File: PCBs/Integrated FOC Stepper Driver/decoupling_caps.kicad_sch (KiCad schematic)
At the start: 12 parts

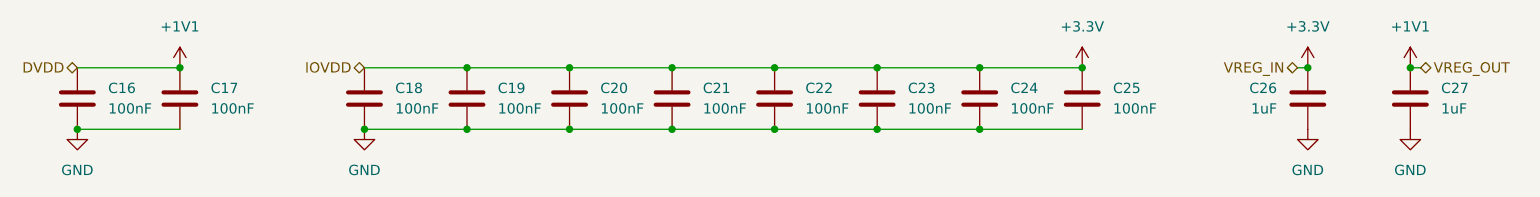
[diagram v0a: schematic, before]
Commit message: Switch to 0805 capacitors instead of stacked 2220 capacitors
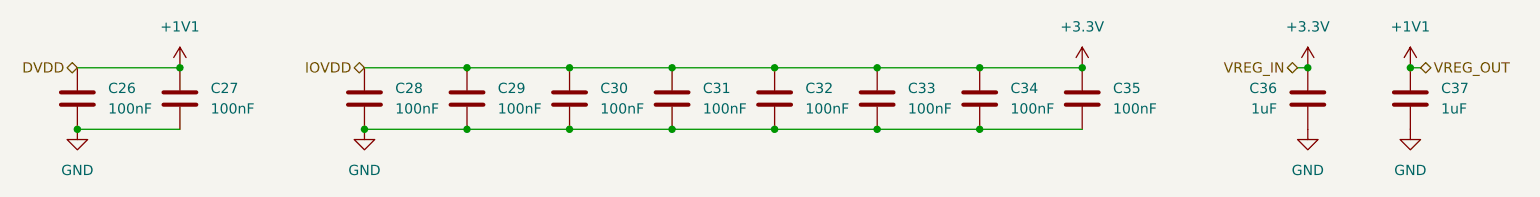
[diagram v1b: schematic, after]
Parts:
- renumbered C16 to C26, C17 to C27, C18 to C28, C19 to C29, C20 to C30, C21 to C31, C22 to C32, C23 to C33, C24 to C34, C25 to C35, C26 to C36, C27 to C37
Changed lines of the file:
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@@
 (kicad_sch
-	(version 20231120)
+	(version 20250114)
 	(generator "eeschema")
-	(generator_version "8.0")
+	(generator_version "9.0")
 	(paper "A4")
 	(junction
@@
 		(dnp no)
 		(fields_autoplaced yes)
-		(property "Reference" "C17"
+		(property "Reference" "C27"
 			(at 40.64 48.2599 0)
 			(effects
@@
 			(project "Integrated FOC Stepper Driver"
 				(path "/d423f88b-f91b-436a-af28-14e717307787/4b2dc276-88ea-42bf-9f9d-08904d070374"
-					(reference "C17")
+					(reference "C27")
 					(unit 1)
 				)
@@
 		(dnp no)
 		(fields_autoplaced yes)
-		(property "Reference" "C16"
+		(property "Reference" "C26"
 			(at 27.94 48.2599 0)
 			(effects
@@
 			(project "Integrated FOC Stepper Driver"
 				(path "/d423f88b-f91b-436a-af28-14e717307787/4b2dc276-88ea-42bf-9f9d-08904d070374"
-					(reference "C16")
+					(reference "C26")
 					(unit 1)
 				)
@@
 		(dnp no)
 		(fields_autoplaced yes)
-		(property "Reference" "C21"
+		(property "Reference" "C31"
 			(at 101.6 48.2599 0)
 			(effects
@@
 			(project "Integrated FOC Stepper Driver"
 				(path "/d423f88b-f91b-436a-af28-14e717307787/4b2dc276-88ea-42bf-9f9d-08904d070374"
-					(reference "C21")
+					(reference "C31")
 					(unit 1)
 				)
@@
 		(dnp no)
 		(fields_autoplaced yes)
-		(property "Reference" "C27"
+		(property "Reference" "C37"
 			(at 193.04 48.2599 0)
 			(effects
@@
 			(project "Integrated FOC Stepper Driver"
 				(path "/d423f88b-f91b-436a-af28-14e717307787/4b2dc276-88ea-42bf-9f9d-08904d070374"
-					(reference "C27")
+					(reference "C37")
 					(unit 1)
 				)
@@
 		(dnp no)
 		(fields_autoplaced yes)
-		(property "Reference" "C24"
+		(property "Reference" "C34"
 			(at 139.7 48.2599 0)
 			(effects
@@
 			(project "Integrated FOC Stepper Driver"
 				(path "/d423f88b-f91b-436a-af28-14e717307787/4b2dc276-88ea-42bf-9f9d-08904d070374"
-					(reference "C24")
+					(reference "C34")
 					(unit 1)
 				)
@@
 		(dnp no)
 		(fields_autoplaced yes)
-		(property "Reference" "C25"
+		(property "Reference" "C35"
 			(at 152.4 48.2599 0)
 			(effects
@@
 			(project "Integrated FOC Stepper Driver"
 				(path "/d423f88b-f91b-436a-af28-14e717307787/4b2dc276-88ea-42bf-9f9d-08904d070374"
-					(reference "C25")
+					(reference "C35")
 					(unit 1)
 				)
@@
 		(dnp no)
 		(fields_autoplaced yes)
-		(property "Reference" "C26"
+		(property "Reference" "C36"
 			(at 172.72 48.2599 0)
 			(effects
@@
 			(project "Integrated FOC Stepper Driver"
 				(path "/d423f88b-f91b-436a-af28-14e717307787/4b2dc276-88ea-42bf-9f9d-08904d070374"
-					(reference "C26")
+					(reference "C36")
 					(unit 1)
 				)
@@
 		(dnp no)
 		(fields_autoplaced yes)
-		(property "Reference" "C18"
+		(property "Reference" "C28"
 			(at 63.5 48.2599 0)
 			(effects
@@
 			(project ""
 				(path "/d423f88b-f91b-436a-af28-14e717307787/4b2dc276-88ea-42bf-9f9d-08904d070374"
-					(reference "C18")
+					(reference "C28")
 					(unit 1)
 				)
@@
 		(dnp no)
 		(fields_autoplaced yes)
-		(property "Reference" "C23"
+		(property "Reference" "C33"
 			(at 127 48.2599 0)
 			(effects
@@
 			(project "Integrated FOC Stepper Driver"
 				(path "/d423f88b-f91b-436a-af28-14e717307787/4b2dc276-88ea-42bf-9f9d-08904d070374"
-					(reference "C23")
+					(reference "C33")
 					(unit 1)
 				)
@@
 		(dnp no)
 		(fields_autoplaced yes)
-		(property "Reference" "C20"
+		(property "Reference" "C30"
 			(at 88.9 48.2599 0)
 			(effects
@@
 			(project "Integrated FOC Stepper Driver"
 				(path "/d423f88b-f91b-436a-af28-14e717307787/4b2dc276-88ea-42bf-9f9d-08904d070374"
-					(reference "C20")
+					(reference "C30")
 					(unit 1)
 				)
@@
 		(dnp no)
 		(fields_autoplaced yes)
-		(property "Reference" "C22"
+		(property "Reference" "C32"
 			(at 114.3 48.2599 0)
 			(effects
@@
 			(project "Integrated FOC Stepper Driver"
 				(path "/d423f88b-f91b-436a-af28-14e717307787/4b2dc276-88ea-42bf-9f9d-08904d070374"
-					(reference "C22")
+					(reference "C32")
 					(unit 1)
 				)
@@
 		(dnp no)
 		(fields_autoplaced yes)
-		(property "Reference" "C19"
+		(property "Reference" "C29"
 			(at 76.2 48.2599 0)
 			(effects
@@
 			(project "Integrated FOC Stepper Driver"
 				(path "/d423f88b-f91b-436a-af28-14e717307787/4b2dc276-88ea-42bf-9f9d-08904d070374"
-					(reference "C19")
-					(unit 1)
-				)
+					(reference "C29")
+					(unit 1)
+				)
